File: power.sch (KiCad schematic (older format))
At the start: 18 parts, among them Q1 NC, U4 RT8070

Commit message: Add the board ID EEPROM chip and move the 0Ohm resistor such that the coin cell battery would actually power SOM_SNVS_3V3 when removed and the NC resistor is populated
This re-arrengment of the resistor makes the reference schematic more clear knowing that SOM_VBAT_3V3 is not actually LICELL.
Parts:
- renumbered C25 to C10, C26 to C11, C27 to C12, C28 to C13, C29 to C14, C30 to C15, C31 to C16, D4 to D1, R18 to R10, R19 to R11, R20 to R12, R21 to R13, R22 to R14, R16 to R8, R17 to R9, U4 to U2
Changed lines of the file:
@@
 $EndDescr
 $Comp
-L R R17
+L R R9
 U 1 1 5AC89121
 P 4700 3100
-F 0 "R17" H 4800 3150 50  0000 C CNN
+F 0 "R9" H 4800 3150 50  0000 C CNN
 F 1 "100k" H 4850 3050 50  0000 C CNN
 F 2 "" V 4630 3100 50  0001 C CNN
@@
 $EndComp
 $Comp
-L C C25
+L C C10
 U 1 1 5AC8916D
 P 4900 3100
-F 0 "C25" H 4925 3200 50  0000 L CNN
+F 0 "C10" H 4925 3200 50  0000 L CNN
 F 1 "10uF" H 4925 3000 50  0000 L CNN
 F 2 "" H 4938 2950 50  0001 C CNN
@@
 $EndComp
 $Comp
-L R R21
+L R R13
 U 1 1 5AC894B5
 P 6750 3100
-F 0 "R21" H 6850 3150 50  0000 C CNN
+F 0 "R13" H 6850 3150 50  0000 C CNN
 F 1 "66k" H 6900 3050 50  0000 C CNN
 F 2 "" V 6680 3100 50  0001 C CNN
@@
 $EndComp
 $Comp
-L R R22
+L R R14
 U 1 1 5AC89505
 P 6750 3500
-F 0 "R22" H 6850 3550 50  0000 C CNN
+F 0 "R14" H 6850 3550 50  0000 C CNN
 F 1 "21.5k" H 6900 3450 50  0000 C CNN
 F 2 "" V 6680 3500 50  0001 C CNN
@@
 $EndComp
 $Comp
-L C C29
+L C C14
 U 1 1 5AC89A9F
 P 7100 3300
-F 0 "C29" H 7125 3400 50  0000 L CNN
+F 0 "C14" H 7125 3400 50  0000 L CNN
 F 1 "47uF" H 7125 3200 50  0000 L CNN
 F 2 "" H 7138 3150 50  0001 C CNN
@@
 $EndComp
 $Comp
-L GND #PWR032
+L GND #PWR031
 U 1 1 5AC89B34
 P 7600 3850
-F 0 "#PWR032" H 7600 3600 50  0001 C CNN
+F 0 "#PWR031" H 7600 3600 50  0001 C CNN
 F 1 "GND" H 7600 3700 50  0000 C CNN
 F 2 "" H 7600 3850 50  0001 C CNN
@@
 $EndComp
 $Comp
-L C C30
+L C C15
 U 1 1 5AC89B6F
 P 7350 3300
-F 0 "C30" H 7375 3400 50  0000 L CNN
+F 0 "C15" H 7375 3400 50  0000 L CNN
 F 1 "47uF" H 7375 3200 50  0000 L CNN
 F 2 "" H 7388 3150 50  0001 C CNN
@@
 $EndComp
 $Comp
-L C C31
+L C C16
 U 1 1 5AC89B9A
 P 7600 3300
-F 0 "C31" H 7625 3400 50  0000 L CNN
+F 0 "C16" H 7625 3400 50  0000 L CNN
 F 1 "47uF" H 7625 3200 50  0000 L CNN
 F 2 "" H 7638 3150 50  0001 C CNN
@@
 $EndComp
 $Comp
-L C C28
+L C C13
 U 1 1 5AC89BD0
 P 6350 3600
-F 0 "C28" H 6375 3700 50  0000 L CNN
+F 0 "C13" H 6375 3700 50  0000 L CNN
 F 1 "560pF" H 6375 3500 50  0000 L CNN
 F 2 "" H 6388 3450 50  0001 C CNN
@@
 $EndComp
 $Comp
-L R R20
+L R R12
 U 1 1 5AC89C89
 P 6150 3400
-F 0 "R20" V 6230 3400 50  0000 C CNN
+F 0 "R12" V 6230 3400 50  0000 C CNN
 F 1 "33k" V 6150 3400 50  0000 C CNN
 F 2 "" V 6080 3400 50  0001 C CNN
@@
 Connection ~ 7600 3800
 $Comp
-L C C27
+L C C12
 U 1 1 5AC8D0FC
 P 6000 4100
-F 0 "C27" H 6025 4200 50  0000 L CNN
+F 0 "C12" H 6025 4200 50  0000 L CNN
 F 1 "10nF" H 6025 4000 50  0000 L CNN
 F 2 "" H 6038 3950 50  0001 C CNN
@@
 	6000 3900 6000 3950
 $Comp
-L GND #PWR033
+L GND #PWR032
 U 1 1 5AC8D19A
 P 6000 4300
-F 0 "#PWR033" H 6000 4050 50  0001 C CNN
+F 0 "#PWR032" H 6000 4050 50  0001 C CNN
 F 1 "GND" H 6000 4150 50  0000 C CNN
 F 2 "" H 6000 4300 50  0001 C CNN
@@
 	6000 4300 6000 4250
 $Comp
-L GND #PWR034
+L GND #PWR033
 U 1 1 5AC8D67B
 P 4900 3300
-F 0 "#PWR034" H 4900 3050 50  0001 C CNN
+F 0 "#PWR033" H 4900 3050 50  0001 C CNN
 F 1 "GND" H 4900 3150 50  0000 C CNN
 F 2 "" H 4900 3300 50  0001 C CNN
@@
 $EndComp
 $Comp
-L VCC_PJ_IN #PWR035
+L VCC_PJ_IN #PWR034
 U 1 1 5AC8DA43
 P 4700 2850
-F 0 "#PWR035" H 4700 2700 50  0001 C CNN
+F 0 "#PWR034" H 4700 2700 50  0001 C CNN
 F 1 "VCC_PJ_IN" H 4700 2990 50  0000 C CNN
 F 2 "" H 4700 2850 50  0001 C CNN
@@
 	4900 3250 4900 3300
 $Comp
-L R R18
+L R R10
 U 1 1 5AC8DBD8
 P 4750 3600
-F 0 "R18" V 4830 3600 50  0000 C CNN
+F 0 "R10" V 4830 3600 50  0000 C CNN
 F 1 "R" V 4750 3600 50  0000 C CNN
 F 2 "" V 4680 3600 50  0001 C CNN
@@
 	4950 3600 4900 3600
 $Comp
-L GND #PWR036
+L GND #PWR035
 U 1 1 5AC8DC4F
 P 4550 3650
-F 0 "#PWR036" H 4550 3400 50  0001 C CNN
+F 0 "#PWR035" H 4550 3400 50  0001 C CNN
 F 1 "GND" H 4550 3500 50  0000 C CNN
 F 2 "" H 4550 3650 50  0001 C CNN
@@
 	4550 3600 4600 3600
 $Comp
-L RT8070 U4
+L RT8070 U2
 U 1 1 5AC8E68B
 P 5450 3400
-F 0 "U4" H 5200 4050 60  0000 C CNN
+F 0 "U2" H 5200 4050 60  0000 C CNN
 F 1 "RT8070" H 5600 4050 60  0000 C CNN
 F 2 "" H 5500 3550 60  0001 C CNN
@@
 $EndComp
 $Comp
-L R R16
+L R R8
 U 1 1 5AC8ED7F
 P 4350 3900
-F 0 "R16" V 4430 3900 50  0000 C CNN
+F 0 "R8" V 4430 3900 50  0000 C CNN
 F 1 "100k" V 4250 3900 50  0000 C CNN
 F 2 "" V 4280 3900 50  0001 C CNN
@@
 $EndComp
 $Comp
-L D_Schottky D4
+L D_Schottky D1
 U 1 1 5AC8EDDE
 P 4550 4100
-F 0 "D4" H 4550 4200 50  0000 C CNN
+F 0 "D1" H 4550 4200 50  0000 C CNN
 F 1 "D_Schottky" H 4550 4000 50  0000 C CNN
 F 2 "" H 4550 4100 50  0001 C CNN
@@
 $EndComp
 $Comp
-L C C26
+L C C11
 U 1 1 5AC8F120
 P 4900 4500
-F 0 "C26" H 4925 4600 50  0000 L CNN
+F 0 "C11" H 4925 4600 50  0000 L CNN
 F 1 "1uF" H 4925 4400 50  0000 L CNN
 F 2 "" H 4938 4350 50  0001 C CNN
@@
 $EndComp
 $Comp
-L R R19
+L R R11
 U 1 1 5AC8F1B3
 P 5150 4500
-F 0 "R19" H 5250 4550 50  0000 C CNN
+F 0 "R11" H 5250 4550 50  0000 C CNN
 F 1 "200k" H 5300 4450 50  0000 C CNN
 F 2 "" V 5080 4500 50  0001 C CNN
@@
 $EndComp
 $Comp
-L SOM_NVCC_3V3 #PWR037
+L SOM_NVCC_3V3 #PWR036
 U 1 1 5AC8F202
 P 4150 3850
-F 0 "#PWR037" H 4150 3700 50  0001 C CNN
+F 0 "#PWR036" H 4150 3700 50  0001 C CNN
 F 1 "SOM_NVCC_3V3" H 4150 3990 50  0000 C CNN
 F 2 "" H 4150 3850 50  0001 C CNN
@@
 Connection ~ 4900 4100
 $Comp
-L GND #PWR038
+L GND #PWR037
 U 1 1 5AC8FABE
 P 4900 4850
-F 0 "#PWR038" H 4900 4600 50  0001 C CNN
+F 0 "#PWR037" H 4900 4600 50  0001 C CNN
 F 1 "GND" H 4900 4700 50  0000 C CNN
 F 2 "" H 4900 4850 50  0001 C CNN
@@
 Connection ~ 4900 4800
 $Comp
-L BASE_PER_3V3 #PWR039
+L BASE_PER_3V3 #PWR038
 U 1 1 5AC95D14
 P 7600 2850
-F 0 "#PWR039" H 7600 2700 50  0001 C CNN
+F 0 "#PWR038" H 7600 2700 50  0001 C CNN
 F 1 "BASE_PER_3V3" H 7600 2990 50  0000 C CNN
 F 2 "" H 7600 2850 50  0001 C CNN
@@
 Connection ~ 7600 2900
 $Comp
-L PWR_FLAG #FLG040
+L PWR_FLAG #FLG039
 U 1 1 5AC9608E
 P 7100 2850
-F 0 "#FLG040" H 7100 2925 50  0001 C CNN
+F 0 "#FLG039" H 7100 2925 50  0001 C CNN
 F 1 "PWR_FLAG" H 7100 3000 50  0000 C CNN
 F 2 "" H 7100 2850 50  0001 C CNN

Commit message: Add reset & watchdog, sd power, and BASE_PER_1V8 circuits
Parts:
- added C12: 1uF, symbol C
- added C15: 4.7uF, symbol C
- added C19: NC, symbol C
- added D2: 30V,100mA, symbol D_Schottky
- added Q2: TPS27082L, symbol TPS27082L
- added Q3: Q_NMOS_DGS, symbol Q_NMOS_DGS
- added R15: 100k, symbol R
- added R16: 10k, symbol R
- added R17: NC, symbol R
- added R18: 49.9, symbol R
- added U3: TLV70218DBVR, symbol TLV70218DBVR
- renumbered C12 to C13, C13 to C14, C14 to C16, C15 to C17, C16 to C18
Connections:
- net labels added: BASE_PER_1V8, NVCC_SD2_1V8_3V3, SW_3P3_SD2, ~CONN_SD2_RST
- wire segments 43 -> 110
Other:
- note added: "1.8V/300mA"
- note added: "3.3V/3A"
- note added: "SD POWER"
- moved on the sheet: 6.8uH1, C10, C11, C13, C14, C16, C17, C18, D1, Q1, R10, R11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

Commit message: Add PTC Fuse, zener on VCC_PJ, USB PD current-limiting switch, 5V regulator, and make regulators' VINA=VIN (since VIH is 1.2V)
Equation for setting NX5P3090's current limit is included.
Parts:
- added C10, C14: C, symbol C
- added L2: L, symbol L
- added R13, R14: R, symbol R
- added U2: RT6150A, symbol RT6150A
- renumbered C10 to C11, C11 to C12, C12 to C13, C13 to C15, C14 to C16, C15 to C17, C16 to C18, C17 to C19, C18 to C20, C19 to C21, D1 to D2, D2 to D3, Q1 to Q2, Q2 to Q3, Q3 to Q4, R9 to R10, R10 to R11, R11 to R12, R12 to R15, R13 to R16, R14 to R17, R15 to R18, R16 to R19, R17 to R20, R18 to R21, R8 to R9, U2 to U3, U3 to U4
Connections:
- net labels added: +5V, VCC_PJ
- net labels removed: VCC_PJ_IN
- wire segments 110 -> 137
- no-connect marks 0 -> 2
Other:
- note added: "5.0V/800mA"
- moved on the sheet: 6.8uH1, C11, C12, C13, C15, C16, C17, C18, C19, C20, C21, D2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

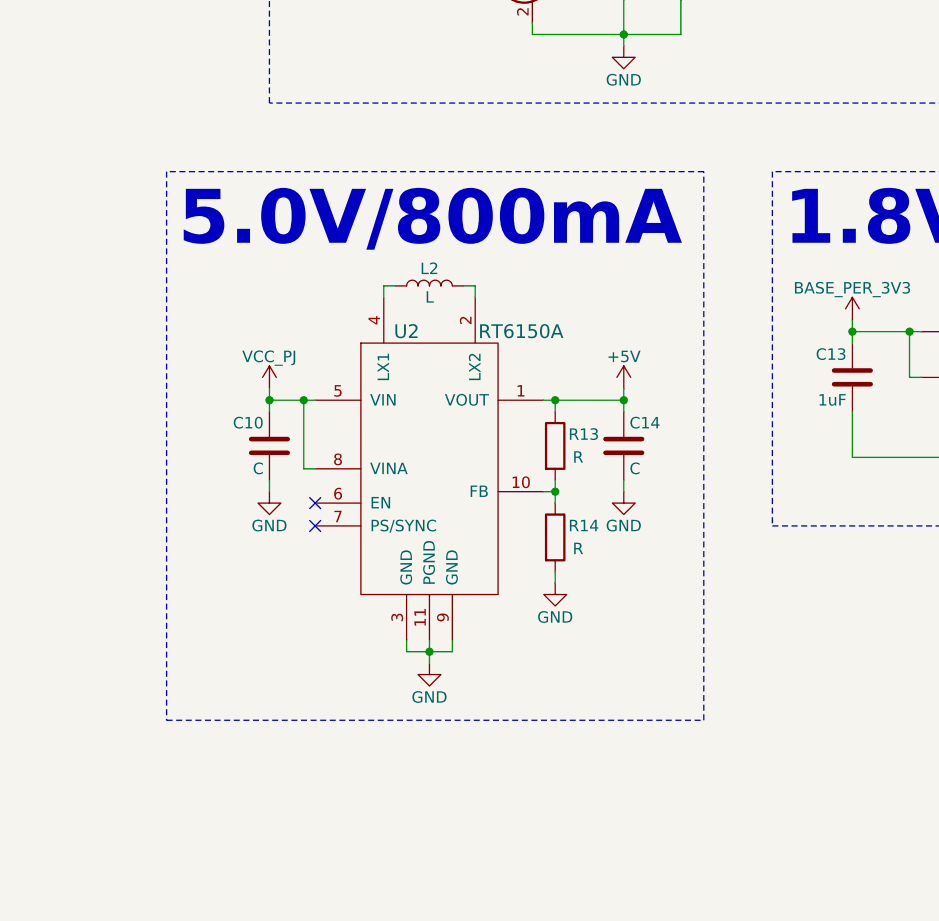
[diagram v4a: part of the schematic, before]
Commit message: Figure out 5.0V buck-boost's inductor value, include inductor current calculations
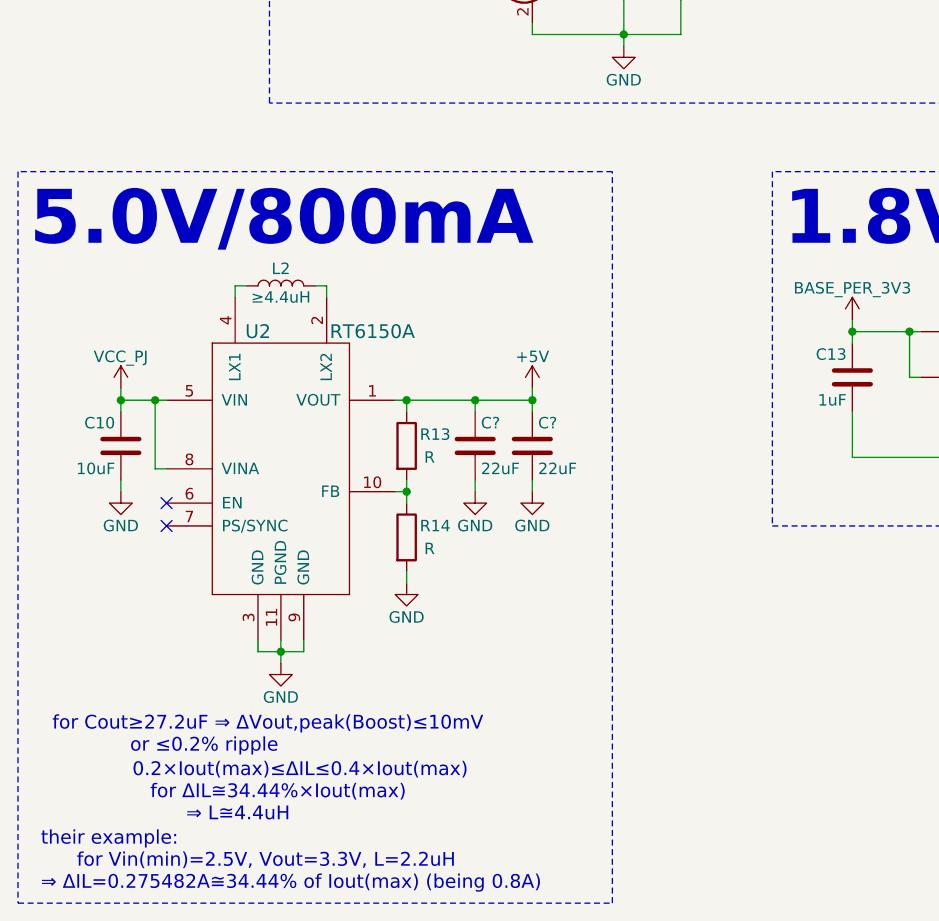
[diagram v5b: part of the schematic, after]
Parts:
- removed C14: C, symbol C
- added C? (x2): 22uF, symbol C
- C10: value C -> 10uF
- L2: value L -> ≥4.4uH
- U2: Distrib Link (none) -> https://www.digikey.com/product-detail/en/richtek-usa-inc/R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; MFG Name (none) -> Richtek; MFG Part Num (none) -> RT6150AGQW; Others (none) -> https://www.digikey.com/products/en/integrated-circuits-ics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; Tolerance (none) -> -
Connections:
- net +5V: now also C?.1, C?.1
- net GND: now also C?.2, C?.2
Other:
- note added: "0.2×Iout(max)≤ΔIL≤0.4×Iout(max)\n for ΔIL≅34.44%×Iout(max)\n ⇒ L≅4.4uH"
- note added: "for Cout≥27.2uF ⇒ ΔVout,peak(Boost)≤10mV\n or ≤0.2% ripple"
- note added: "their example:\n for Vin(min)=2.5V, Vout=3.3V, L=2.2uH\n⇒ ΔIL=0.275482A≅34.44% of Iout(max) (being 0.8A)"
- moved on the sheet: C10, L2, R13, R14, U2

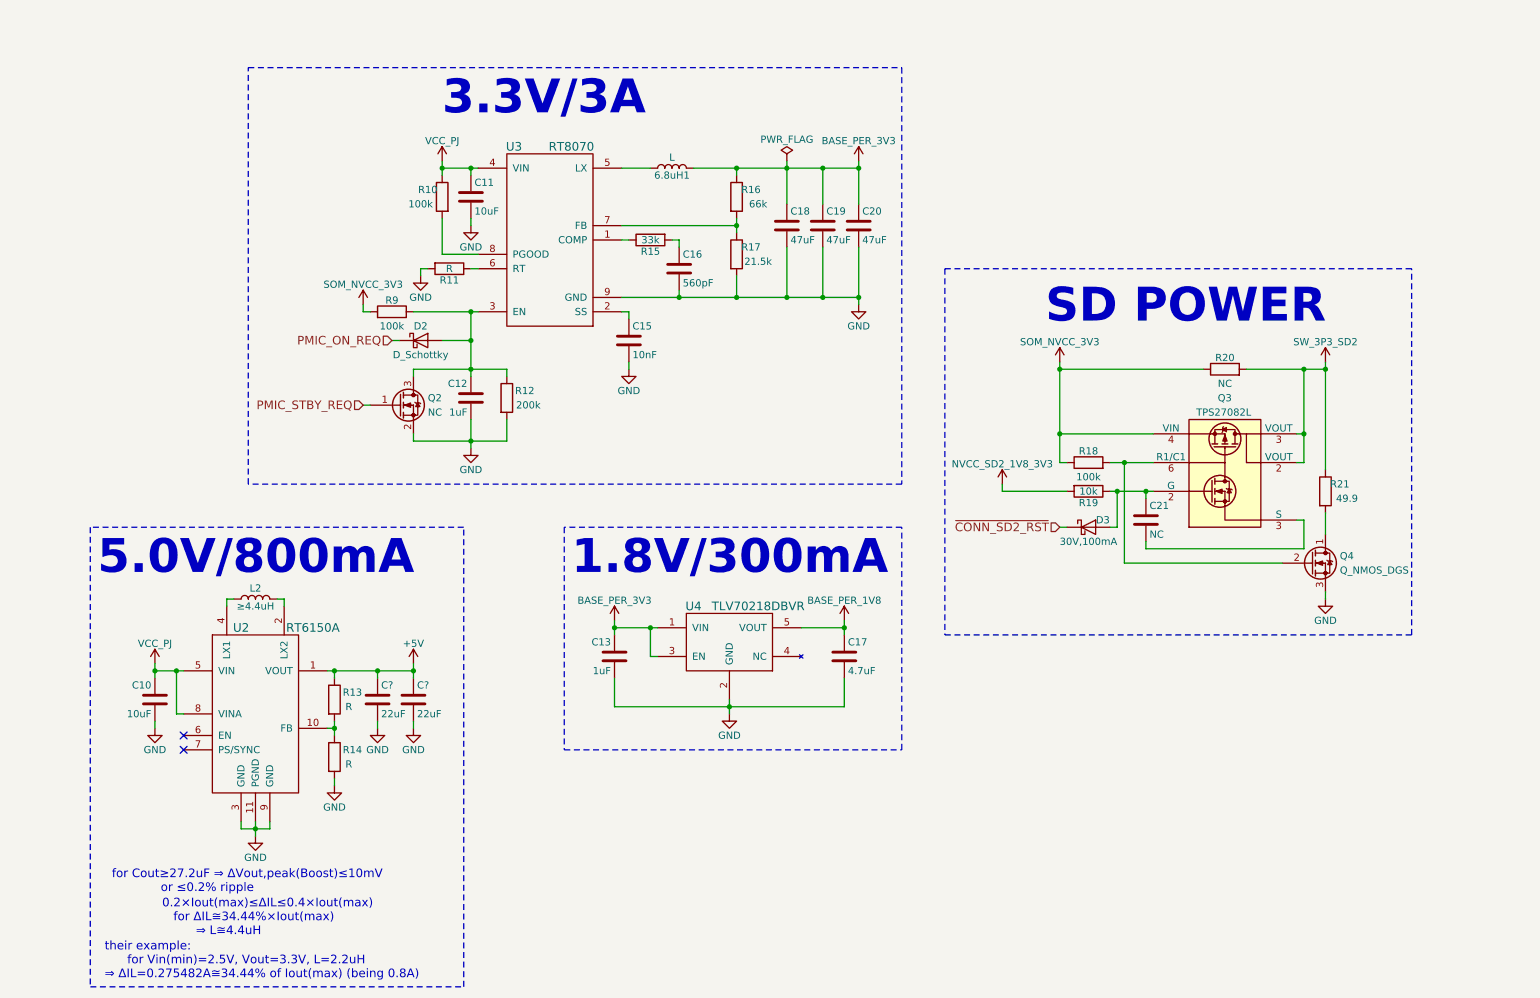
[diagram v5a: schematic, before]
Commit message: Use MIC2876 instead of RT6150A due to several advantages which are noted in the schematic
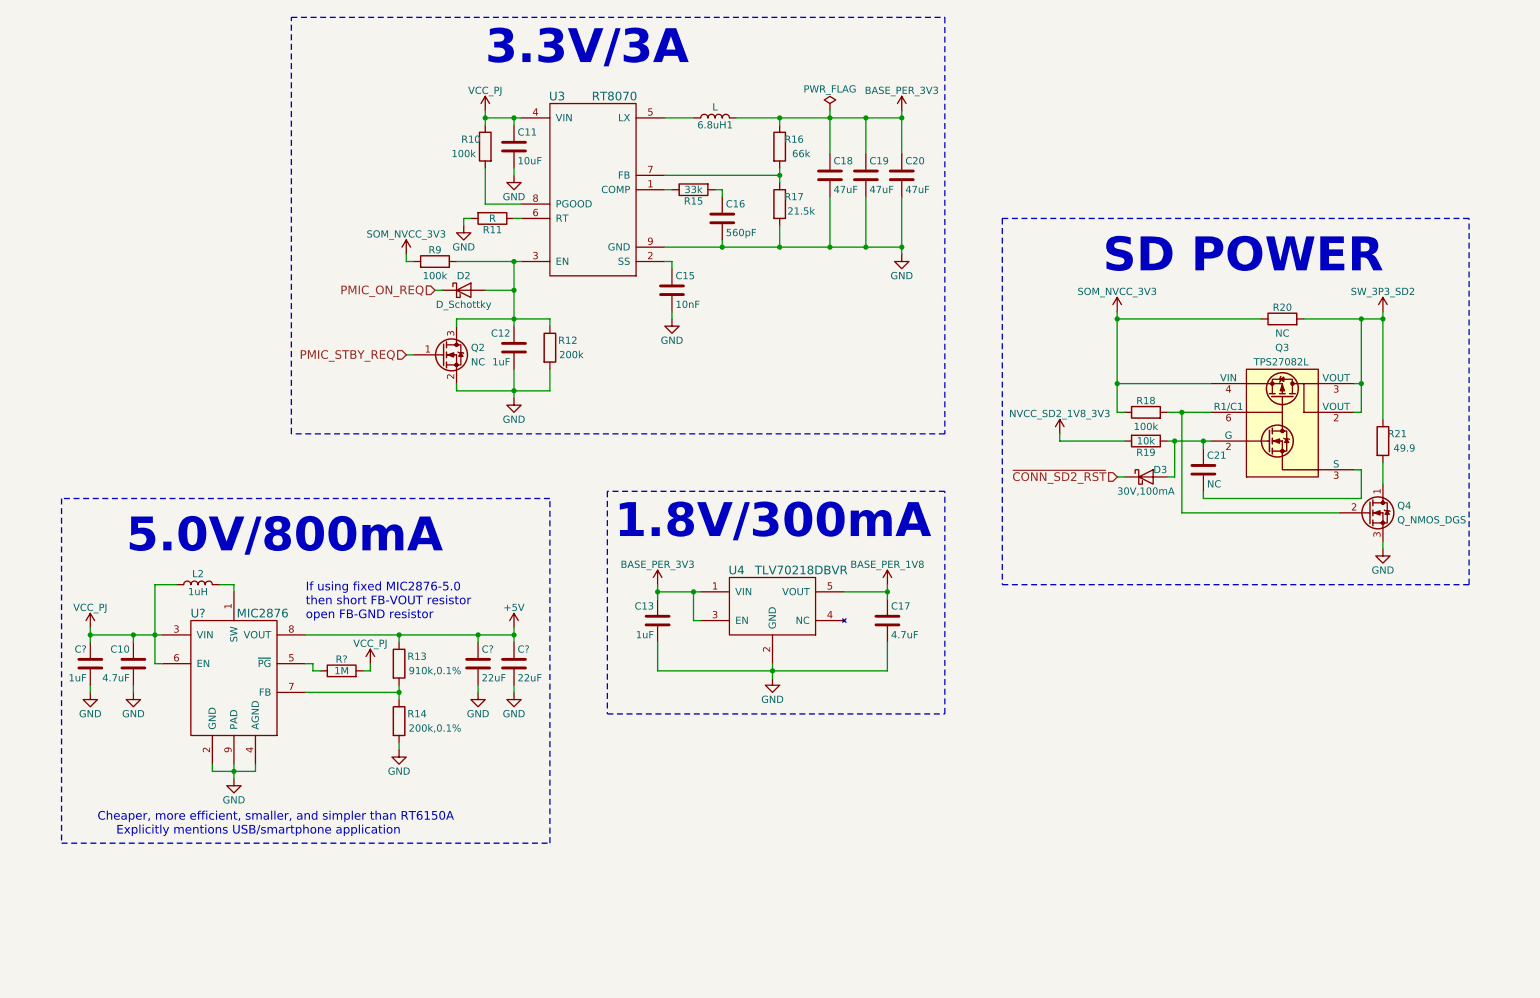
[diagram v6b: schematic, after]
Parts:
- removed C?: 22uF, symbol C
- removed U2: RT6150A, symbol RT6150A
- added C?: 22uF, Capacitors_SMD:C_0805, symbol C
- added C?: 1uF, symbol C
- added R?: 1M, symbol R
- added U?: MIC2876, symbol MIC2876
- C10: value 10uF -> 4.7uF; Distrib Link (none) -> https://www.digikey.com/product-detail/en/taiyo-yuden/LMK10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; Distrib Name (none) -> Taiyo Yuden; Distrib PN (none) -> 587-1441-1-ND; MFG Part Num (none) -> LMK107BJ475KA-T; Others (none) -> https://www.digikey.com/products/en/capacitors/ceramic-capa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; Tolerance (none) -> -
- C?: footprint (none) -> Capacitors_SMD:C_0805; Distrib Link https://www.digikey.com/product-detail/en/murata-electronic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 -> https://www.digikey.com/product-detail/en/taiyo-yuden/LMK21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; Distrib PN 490-10476-1-ND -> 587-5464-1-ND; MFG Name Murata -> Taiyo Yuden; MFG Part Num GRM188R61A226ME15D -> LMK212BBJ226MG-T; Others https://www.digikey.com/products/en/capacitors/ceramic-capacitors/60?FV=c0005%2C380001%2C38042a%2C38006f%2C380467%2C380071%2C380474%2C380475%2C380477%2C3804da%2C3804ef%2C380513%2C380514%2C380085%2C38054c%2C38055b%2C38055c%2C38055e%2C38055f%2C380560%2C380577%2C38000e%2C38058f%2C380590%2C380591%2C380592%2C380090%2C3805e1%2C3805e2%2C3805e5%2C3805e6%2C3805e9%2C3805f2%2C380010%2C380012%2C3800bd%2C380766%2C3800c0%2C380002%2C380014%2C3800cf%2C380016%2C380018%2C38001a%2C38010c%2C38001c%2C380132%2C38001f%2C380020%2C380022%2C380026%2C380004%2C38002e%2C3801ec%2C3801f9%2C380035%2C380253%2C38029f%2C3802a0%2C3802a1%2C3802a2%2C3802a3%2C3802a5%2C3802a6%2C380306%2C380307%2C380009%2C38038f%2C400005%2C440013%2Cb89a25%2C1f140000%2Cmu22%C2%B5F%7C2049%2Cffe0003c&quantity=0&ColumnSort=1000011&page=1&pageSize=500 -> https://www.digikey.com/products/en/capacitors/ceramic-capacitors/60?k=&pkeyword=&pv14=4&FV=400006%2C440013%2C1f140000%2Cmu22%C2%B5F%7C2049%2Cffe0003c&quantity=0&ColumnSort=1000011&page=1&pageSize=500
- L2: value ≥4.4uH -> 1uH; Distrib Link (none) -> https://www.mouser.com/ProductDetail/Coilcraft/XAL4020-102M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; Distrib PN (none) -> 994-XAL4020-102MEC; MFG Name (none) -> Coilcraft; MFG Part Num (none) -> XAL4020-102MEC; Others (none) -> https://www.mouser.com/ProductDetail/Coilcraft/XAL4020-102M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; Tolerance (none) -> -
- R13: value R -> 910k,0.1%
- R14: value R -> 200k,0.1%
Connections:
- net +5V: now also C?.1, U?.8 (VOUT)
- net GND: now also C?.2, C?.2, U?.2 (GND), U?.4 (AGND), U?.9 (PAD)
- net VCC_PJ: now also L2.1, C?.1, R?.2, U?.3 (VIN), U?.6 (EN)
- net at R13.2, R14.1: now also U?.7 (FB)
- net at L2.2: now also U?.1 (SW)
- new net: R?.1, U?.5 (~PG)
- no-connect marks 2 -> 0
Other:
- note added: "Cheaper, more efficient, smaller, and simpler than RT6150A\n Explicitly mentions USB/smartphone application"
- note added: "If using fixed MIC2876-5.0\nthen short FB-VOUT resistor\nopen FB-GND resistor"
- note removed: "0.2×Iout(max)≤ΔIL≤0.4×Iout(max)\n for ΔIL≅34.44%×Iout(max)\n ⇒ L≅4.4uH"
- note removed: "for Cout≥27.2uF ⇒ ΔVout,peak(Boost)≤10mV\n or ≤0.2% ripple"
- note removed: "their example:\n for Vin(min)=2.5V, Vout=3.3V, L=2.2uH\n⇒ ΔIL=0.275482A≅34.44% of Iout(max) (being 0.8A)"
- moved on the sheet: 6.8uH1, C10, C11, C12, C13, C15, C16, C17, C18, C19, C20, C21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
